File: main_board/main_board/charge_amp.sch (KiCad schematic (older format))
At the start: 17 parts, among them U2 TLV2771CDBVT, U3 TLV2771CDBVT, U4 TLV2771CDBVT

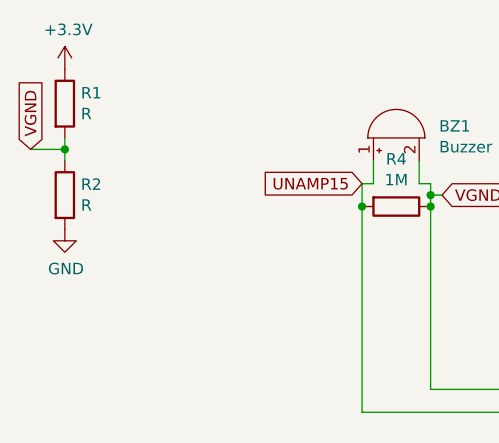
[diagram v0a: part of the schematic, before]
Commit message: re added teensy footprints
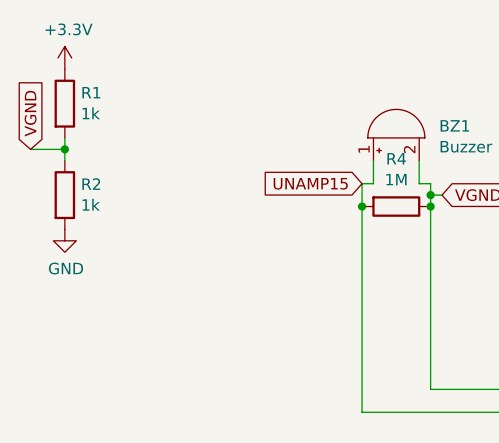
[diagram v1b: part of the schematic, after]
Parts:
- R1, R2: value R -> 1k
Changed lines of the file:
@@
 P 850 1200
 F 0 "R1" H 920 1246 50  0000 L CNN
-F 1 "R" H 920 1155 50  0000 L CNN
+F 1 "1k" H 920 1155 50  0000 L CNN
 F 2 "exocam_charge_amp:0603_R" V 780 1200 50  0001 C CNN
 F 3 "~" H 850 1200 50  0001 C CNN
@@
 P 850 1600
 F 0 "R2" H 920 1646 50  0000 L CNN
-F 1 "R" H 920 1555 50  0000 L CNN
+F 1 "1k" H 920 1555 50  0000 L CNN
 F 2 "exocam_charge_amp:0603_R" V 780 1600 50  0001 C CNN
 F 3 "~" H 850 1600 50  0001 C CNN

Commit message: updated daughter board schematic
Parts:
- U2, U3, U4: symbol exocam_charge_amp:TLV2771CDBVT -> main_board-rescue:TLV2771CDBVT-exocam_charge_amp
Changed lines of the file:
@@
 $EndDescr
 $Comp
-L exocam_charge_amp:TLV2771CDBVT U2
+L main_board-rescue:TLV2771CDBVT-exocam_charge_amp U2
 U 1 1 60F4268F
 P 3900 2000
+AR Path="/60F4268F" Ref="U2"  Part="1"
+AR Path="/60F3F468/60F4268F" Ref="U2"  Part="1"
 F 0 "U2" H 3925 2215 50  0000 C CNN
 F 1 "TLV2771CDBVT" H 3925 2124 50  0000 C CNN
@@
 $EndComp
 $Comp
-L exocam_charge_amp-cache:+3.3V #PWR0117
+L main_board-rescue:+3.3V-exocam_charge_amp-cache #PWR0117
 U 1 1 60F44497
 P 4400 2050
@@
 	850  1350 850  1400
 $Comp
-L exocam_charge_amp-cache:+3.3V #PWR0119
+L main_board-rescue:+3.3V-exocam_charge_amp-cache #PWR0119
 U 1 1 60F49067
 P 850 1050
@@
 UNAMP15
 $Comp
-L exocam_charge_amp:TLV2771CDBVT U3
+L main_board-rescue:TLV2771CDBVT-exocam_charge_amp U3
 U 1 1 60F66909
 P 3900 4150
+AR Path="/60F66909" Ref="U3"  Part="1"
+AR Path="/60F3F468/60F66909" Ref="U3"  Part="1"
 F 0 "U3" H 3925 4365 50  0000 C CNN
 F 1 "TLV2771CDBVT" H 3925 4274 50  0000 C CNN
@@
 $EndComp
 $Comp
-L exocam_charge_amp-cache:+3.3V #PWR0121
+L main_board-rescue:+3.3V-exocam_charge_amp-cache #PWR0121
 U 1 1 60F6691B
 P 4400 4200
@@
 UNAMP16
 $Comp
-L exocam_charge_amp:TLV2771CDBVT U4
+L main_board-rescue:TLV2771CDBVT-exocam_charge_amp U4
 U 1 1 60F6A561
 P 7050 2050
+AR Path="/60F6A561" Ref="U4"  Part="1"
+AR Path="/60F3F468/60F6A561" Ref="U4"  Part="1"
 F 0 "U4" H 7075 2265 50  0000 C CNN
 F 1 "TLV2771CDBVT" H 7075 2174 50  0000 C CNN
@@
 $EndComp
 $Comp
-L exocam_charge_amp-cache:+3.3V #PWR0123
+L main_board-rescue:+3.3V-exocam_charge_amp-cache #PWR0123
 U 1 1 60F6A573
 P 7550 2100

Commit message: edited daughter board schematic slightly to include the latest push button addition
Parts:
- BZ1, BZ2, BZ3: symbol Device:Buzzer -> main_board-rescue:Buzzer-Device
- C1, C2, C3: symbol Device:C -> main_board-rescue:C-Device
- R1, R2, R3, R4, R5, R6, R7, R8: symbol Device:R -> main_board-rescue:R-Device
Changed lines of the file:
@@
 $EndComp
 $Comp
-L Device:C C1
+L main_board-rescue:C-Device C1
 U 1 1 60F42E52
 P 3900 2950
@@
 $EndComp
 $Comp
-L Device:R R3
+L main_board-rescue:R-Device R3
 U 1 1 60F43CAE
 P 3900 3350
@@
 	3100 2200 3600 2200
 $Comp
-L Device:Buzzer BZ1
+L main_board-rescue:Buzzer-Device BZ1
 U 1 1 60F46701
 P 2300 1350
+AR Path="/60F46701" Ref="BZ1"  Part="1"
+AR Path="/60F3F468/60F46701" Ref="BZ1"  Part="1"
 F 0 "BZ1" V 2351 1163 50  0000 R CNN
 F 1 "Buzzer" V 2260 1163 50  0000 R CNN
@@
 $EndComp
 $Comp
-L Device:R R1
+L main_board-rescue:R-Device R1
 U 1 1 60F473D1
 P 850 1200
@@
 $EndComp
 $Comp
-L Device:R R2
+L main_board-rescue:R-Device R2
 U 1 1 60F47F6A
 P 850 1600
@@
 $EndComp
 $Comp
-L Device:R R4
+L main_board-rescue:R-Device R4
 U 1 1 60F4A76F
 P 2300 1650
@@
 $EndComp
 $Comp
-L Device:C C2
+L main_board-rescue:C-Device C2
 U 1 1 60F6690F
 P 3900 5100
@@
 $EndComp
 $Comp
-L Device:R R6
+L main_board-rescue:R-Device R6
 U 1 1 60F66915
 P 3900 5500
@@
 	3100 4350 3600 4350
 $Comp
-L Device:Buzzer BZ2
+L main_board-rescue:Buzzer-Device BZ2
 U 1 1 60F6692A
 P 2300 3500
+AR Path="/60F6692A" Ref="BZ2"  Part="1"
+AR Path="/60F3F468/60F6692A" Ref="BZ2"  Part="1"
 F 0 "BZ2" V 2351 3313 50  0000 R CNN
 F 1 "Buzzer" V 2260 3313 50  0000 R CNN
@@
 $EndComp
 $Comp
-L Device:R R5
+L main_board-rescue:R-Device R5
 U 1 1 60F66930
 P 2300 3800
@@
 $EndComp
 $Comp
-L Device:C C3
+L main_board-rescue:C-Device C3
 U 1 1 60F6A567
 P 7050 3000
@@
 $EndComp
 $Comp
-L Device:R R8
+L main_board-rescue:R-Device R8
 U 1 1 60F6A56D
 P 7050 3400
@@
 	6250 2250 6750 2250
 $Comp
-L Device:Buzzer BZ3
+L main_board-rescue:Buzzer-Device BZ3
 U 1 1 60F6A582
 P 5450 1400
+AR Path="/60F6A582" Ref="BZ3"  Part="1"
+AR Path="/60F3F468/60F6A582" Ref="BZ3"  Part="1"
 F 0 "BZ3" V 5501 1213 50  0000 R CNN
 F 1 "Buzzer" V 5410 1213 50  0000 R CNN
@@
 $EndComp
 $Comp
-L Device:R R7
+L main_board-rescue:R-Device R7
 U 1 1 60F6A588
 P 5450 1700
